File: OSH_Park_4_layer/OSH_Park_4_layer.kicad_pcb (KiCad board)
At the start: 2 copper layers, 2 parts

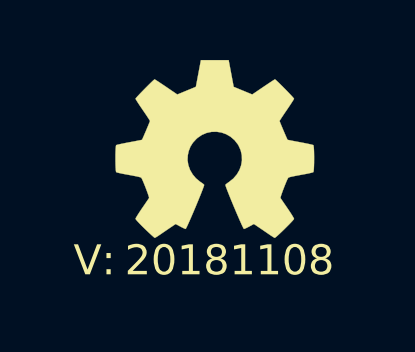
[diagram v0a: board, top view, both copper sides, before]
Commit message: updated via sizes, updated layers, updated plotting settings
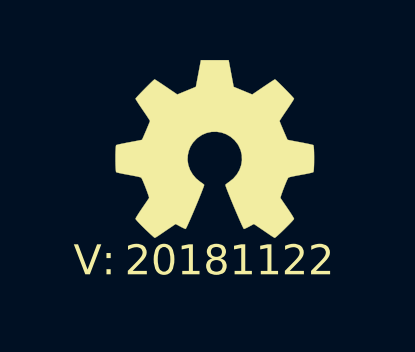
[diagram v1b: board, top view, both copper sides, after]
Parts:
- N2: value 20181108 -> 20181122
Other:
- copper layers 2 -> 4
- net class Default: clearance 0.1524 -> 0.127; trace_width 0.1524 -> 0.127; via_dia 0.381 -> 0.3556
- rule trace_clearance: 0.1524 -> 0.127
- rule trace_min: 0.1524 -> 0.127
- rule via_min_size: 0.381 -> 0.3556
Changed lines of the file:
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@@
   (layers
     (0 F.Cu signal)
+    (1 In1.Cu signal)
+    (2 In2.Cu signal)
     (31 B.Cu signal)
     (32 B.Adhes user)
@@
   )
   (setup
-    (last_trace_width 0.1524)
-    (user_trace_width 0.1524)
+    (last_trace_width 0.127)
+    (user_trace_width 0.127)
     (user_trace_width 0.2)
     (user_trace_width 0.3)
@@
     (user_trace_width 1.5)
     (user_trace_width 2)
-    (trace_clearance 0.1524)
+    (trace_clearance 0.127)
     (zone_clearance 0.508)
     (zone_45_only no)
-    (trace_min 0.1524)
+    (trace_min 0.127)
     (segment_width 0.2)
     (edge_width 0.15)
-    (via_size 0.381)
+    (via_size 0.3556)
     (via_drill 0.254)
-    (via_min_size 0.381)
+    (via_min_size 0.3556)
     (via_min_drill 0.254)
-    (user_via 0.381 0.254)
-    (user_via 0.55 0.4)
-    (user_via 0.75 0.6)
-    (user_via 0.95 0.8)
+    (user_via 0.4 0.254)
+    (user_via 0.6 0.4)
+    (user_via 0.8 0.6)
+    (user_via 1 0.8)
     (user_via 1.3 1)
     (user_via 1.5 1.2)
     (user_via 1.7 1.4)
     (user_via 1.9 1.6)
-    (uvia_size 0.381)
+    (uvia_size 0.3556)
     (uvia_drill 0.254)
     (uvias_allowed no)
-    (uvia_min_size 0.381)
+    (uvia_min_size 0.3556)
     (uvia_min_drill 0.254)
     (pcb_text_width 0.3)
@@
     (visible_elements FFFFFF7F)
     (pcbplotparams
-      (layerselection 0x00030_80000001)
-      (usegerberextensions false)
+      (layerselection 0x010fc_ffffffff)
+      (usegerberextensions true)
       (usegerberattributes false)
       (usegerberadvancedattributes false)
@@
       (outputformat 1)
       (mirror false)
-      (drillshape 1)
+      (drillshape 0)
       (scaleselection 1)
-      (outputdirectory ""))
+      (outputdirectory "OSH_Park_4_layer_plots"))
   )
   (net 0 "")
   (net_class Default "This is the default net class."
-    (clearance 0.1524)
-    (trace_width 0.1524)
-    (via_dia 0.381)
+    (clearance 0.127)
+    (trace_width 0.127)
+    (via_dia 0.3556)
     (via_drill 0.254)
-    (uvia_dia 0.381)
+    (uvia_dia 0.3556)
     (uvia_drill 0.254)
   )
@@
       (effects (font (size 1 1) (thickness 0.15)))
     )
-    (fp_text value 20181108 (at -0.4 -0.1) (layer F.SilkS)
-      (effects (font (size 1 1) (thickness 0.15)))
-    )
+    (fp_text value 20181122 (at -0.4 -0.1) (layer F.SilkS)
+      (effects (font (size 1 1) (thickness 0.15)))
+    )

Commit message: updated paste vs pad ratio, updated soldermask clearance
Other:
- rule pad_to_mask_clearance: 0.2 -> 0.1
- rule solder_mask_min_width: 0.25 -> 0.1
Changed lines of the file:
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@@
-(kicad_pcb (version 20171130) (host pcbnew 5.0.1-33cea8e~68~ubuntu18.04.1)
+(kicad_pcb (version 20171130) (host pcbnew 5.0.2-bee76a0~70~ubuntu18.04.1)
   (general
     (thickness 1.6)
@@
     (pad_size 1.524 1.524)
     (pad_drill 0.762)
-    (pad_to_mask_clearance 0.2)
-    (solder_mask_min_width 0.25)
+    (pad_to_mask_clearance 0.1)
+    (solder_mask_min_width 0.1)
+    (pad_to_paste_clearance_ratio 0.15)
     (aux_axis_origin 0 0)
     (visible_elements FFFFFF7F)

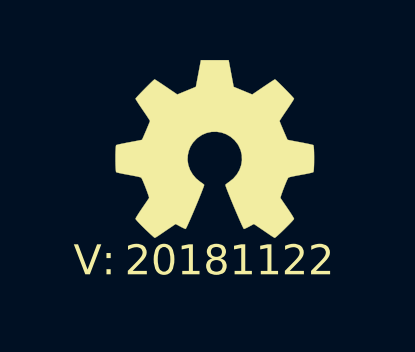
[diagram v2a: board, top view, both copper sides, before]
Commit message: updated solderpaste expansion to 0%
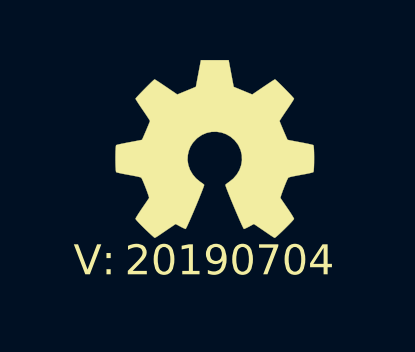
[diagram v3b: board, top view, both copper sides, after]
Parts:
- N2: value 20181122 -> 20190704
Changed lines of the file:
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@@
-(kicad_pcb (version 20171130) (host pcbnew 5.0.2-bee76a0~70~ubuntu18.04.1)
+(kicad_pcb (version 20171130) (host pcbnew 5.1.2-f72e74a~84~ubuntu18.04.1)
   (general
     (thickness 1.6)
@@
     (zone_45_only no)
     (trace_min 0.127)
-    (segment_width 0.2)
-    (edge_width 0.15)
     (via_size 0.3556)
     (via_drill 0.254)
@@
     (uvia_min_size 0.3556)
     (uvia_min_drill 0.254)
+    (edge_width 0.15)
+    (segment_width 0.2)
     (pcb_text_width 0.3)
     (pcb_text_size 1.5 1.5)
@@
     (pad_to_mask_clearance 0.1)
     (solder_mask_min_width 0.1)
-    (pad_to_paste_clearance_ratio 0.15)
     (aux_axis_origin 0 0)
     (visible_elements FFFFFF7F)
@@
       (effects (font (size 1 1) (thickness 0.15)))
     )
-    (fp_text value 20181122 (at -0.4 -0.1) (layer F.SilkS)
-      (effects (font (size 1 1) (thickness 0.15)))
-    )
+    (fp_text value 20190704 (at -0.4 -0.1) (layer F.SilkS)
+      (effects (font (size 1 1) (thickness 0.15)))
+    )

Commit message: updated font sizes to 0.8mm height and 0.15mm line thickness
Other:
- net class Default removed
